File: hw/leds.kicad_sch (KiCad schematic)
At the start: 8 parts, among them Q4 SSM6N35AFE

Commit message: layout finished (draft)
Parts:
- added D7 (x2): LED_BARG, proj_footprints:LED_RGB_2504_horiz_barg, symbol Device:LED_BARG
- added Q4 (x4): SSM6N35AFE, proj_footprints:SOT-563-adjusted, symbol Device:Q_Dual_NMOS_S1G1D2S2G2D1
- added R10 (x2): 750, Resistor_SMD:R_0603_1608Metric, symbol Device:R_Small
- added R9 (x2): 2k, Resistor_SMD:R_0603_1608Metric, symbol Device:R_Small
- added R98 (x2): 230, Resistor_SMD:R_0603_1608Metric, symbol Device:R_Small
- Q4: symbol Device:Q_DUAL_NMOS_S1G1D2S2G2D1 -> Device:Q_Dual_NMOS_S1G1D2S2G2D1
- Q4: symbol Device:Q_DUAL_NMOS_S1G1D2S2G2D1 -> Device:Q_Dual_NMOS_S1G1D2S2G2D1; Manufacturer Toshiba -> (none)
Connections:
- net +5V: now also D7.2 (A), D7.2 (A)
- net GND: now also Q4.1 (S), Q4.1 (S), Q4.1 (S), Q4.1 (S), Q4.4 (S), Q4.4 (S)
- new net: D7.3 (RK), R10.1 (x2)
- new net: Q4.6 (D), R10.2
- new net: D7.1 (BK), R98.1 (x2)
- new net: D7.4 (GK), R9.1 (x2)
- new net: Q4.6 (D), R9.2 (x2)
- new net: Q4.3 (D), R98.2
- new net: Q4.6 (D), R98.2
- new net: Q4.3 (D), R10.2
- new net LED_CHA_B: Q4.2 (G)
- new net LED_CHA_G: Q4.2 (G)
- new net LED_CHA_R: Q4.5 (G)
- new net LED_CHB_B: Q4.5 (G)
- new net LED_CHB_G: Q4.2 (G)
- new net LED_CHB_R: Q4.2 (G)

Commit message: finished routing; DRC passes (except for 1 hole violation at push-button)
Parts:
- Q4: Manufacturer (none) -> Toshiba; Part (none) -> SSM6N35AFE
- Q4: Part (none) -> SSM6N35AFE
- R24: Manufacturer Yageo -> (none); Part RT0603FRE0710KL -> (none)
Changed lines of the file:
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@@
       (effects (font (size 1.27 1.27)) hide)
     )
-    (property "Part" "RT0603FRE0710KL" (at 95.885 40.005 90)
-      (effects (font (size 1.27 1.27)) hide)
-    )
-    (property "Manufacturer" "Yageo" (at 95.885 40.005 90)
+    (property "Part" "" (at 95.885 40.005 90)
+      (effects (font (size 1.27 1.27)) hide)
+    )
+    (property "Manufacturer" "" (at 95.885 40.005 90)
       (effects (font (size 1.27 1.27)) hide)
     )
@@
     )
     (property "Datasheet" "~" (at 177.8 116.84 0)
+      (effects (font (size 1.27 1.27)) hide)
+    )
+    (property "Manufacturer" "Toshiba" (at 172.72 116.84 0)
+      (effects (font (size 1.27 1.27)) hide)
+    )
+    (property "Part" "SSM6N35AFE" (at 172.72 116.84 0)
       (effects (font (size 1.27 1.27)) hide)
     )
@@
       (effects (font (size 1.27 1.27)) hide)
     )
+    (property "Manufacturer" "Toshiba" (at 80.645 135.89 0)
+      (effects (font (size 1.27 1.27)) hide)
+    )
+    (property "Part" "SSM6N35AFE" (at 80.645 135.89 0)
+      (effects (font (size 1.27 1.27)) hide)
+    )
     (pin "1")
     (pin "2")
@@
       (effects (font (size 1.27 1.27)) hide)
     )
+    (property "Part" "SSM6N35AFE" (at 80.645 56.515 0)
+      (effects (font (size 1.27 1.27)) hide)
+    )
     (pin "1")
     (pin "2")
@@
       (effects (font (size 1.27 1.27)) hide)
     )
+    (property "Manufacturer" "Toshiba" (at 80.645 116.84 0)
+      (effects (font (size 1.27 1.27)) hide)
+    )
+    (property "Part" "SSM6N35AFE" (at 80.645 116.84 0)
+      (effects (font (size 1.27 1.27)) hide)
+    )
     (pin "1")
     (pin "2")
@@
       (effects (font (size 1.27 1.27)) hide)
     )
+    (property "Manufacturer" "Toshiba" (at 80.645 94.615 0)
+      (effects (font (size 1.27 1.27)) hide)
+    )
+    (property "Part" "SSM6N35AFE" (at 80.645 94.615 0)
+      (effects (font (size 1.27 1.27)) hide)
+    )
     (pin "1")
     (pin "2")
@@
       (effects (font (size 1.27 1.27)) hide)
     )
+    (property "Manufacturer" "Toshiba" (at 80.645 75.565 0)
+      (effects (font (size 1.27 1.27)) hide)
+    )
+    (property "Part" "SSM6N35AFE" (at 80.645 75.565 0)
+      (effects (font (size 1.27 1.27)) hide)
+    )
     (pin "1")
     (pin "2")
@@
       (effects (font (size 1.27 1.27)) hide)
     )
+    (property "Manufacturer" "Toshiba" (at 172.72 154.94 0)
+      (effects (font (size 1.27 1.27)) hide)
+    )
+    (property "Part" "SSM6N35AFE" (at 172.72 154.94 0)
+      (effects (font (size 1.27 1.27)) hide)
+    )
     (pin "1")
     (pin "2")
@@
       (effects (font (size 1.27 1.27)) hide)
     )
+    (property "Manufacturer" "Toshiba" (at 80.645 154.94 0)
+      (effects (font (size 1.27 1.27)) hide)
+    )
+    (property "Part" "SSM6N35AFE" (at 80.645 154.94 0)
+      (effects (font (size 1.27 1.27)) hide)
+    )
     (pin "1")
     (pin "2")
@@
       (effects (font (size 1.27 1.27)) hide)
     )
+    (property "Manufacturer" "Toshiba" (at 172.72 135.89 0)
+      (effects (font (size 1.27 1.27)) hide)
+    )
+    (property "Part" "SSM6N35AFE" (at 172.72 135.89 0)
+      (effects (font (size 1.27 1.27)) hide)
+    )
     (pin "1")
     (pin "2")
@@
       (effects (font (size 1.27 1.27)) hide)
     )
+    (property "Manufacturer" "Toshiba" (at 81.915 37.465 0)
+      (effects (font (size 1.27 1.27)) hide)
+    )
+    (property "Part" "SSM6N35AFE" (at 81.915 37.465 0)
+      (effects (font (size 1.27 1.27)) hide)
+    )

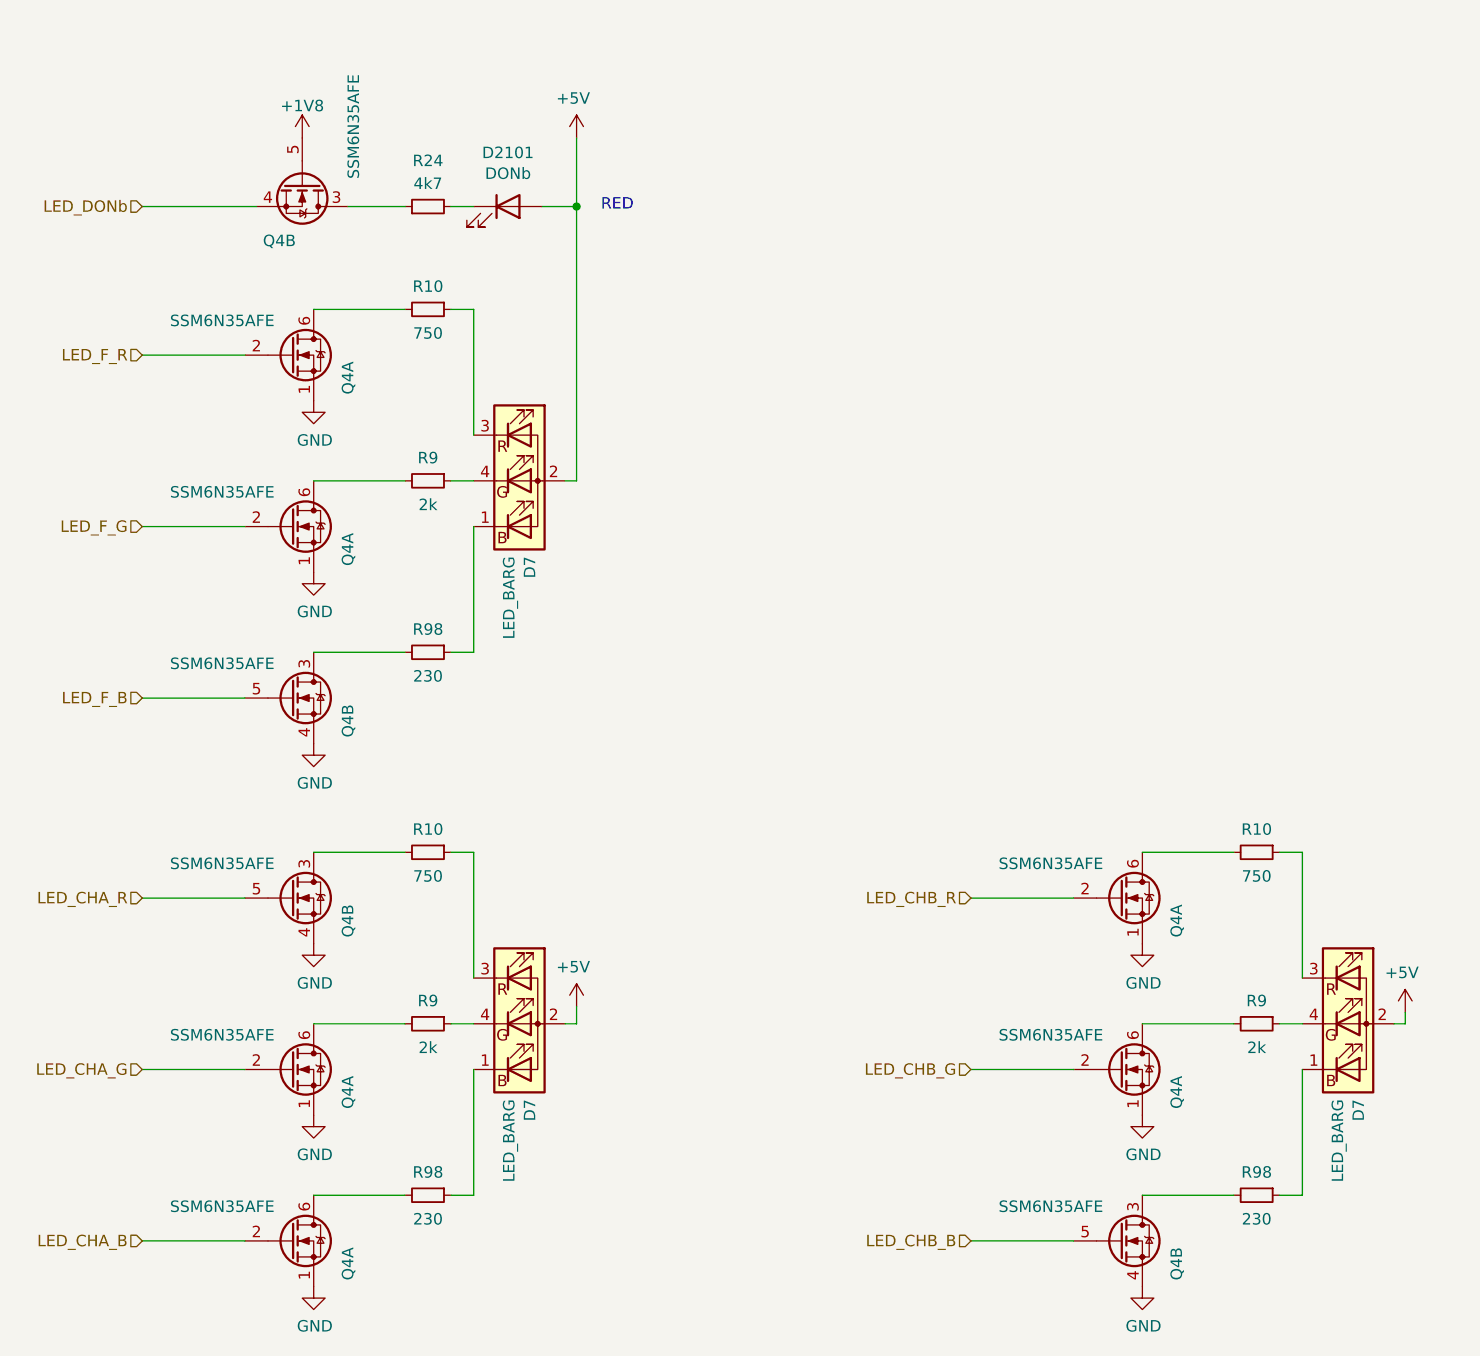
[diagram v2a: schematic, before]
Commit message: added 2nd front led; more keepouts around signal lines
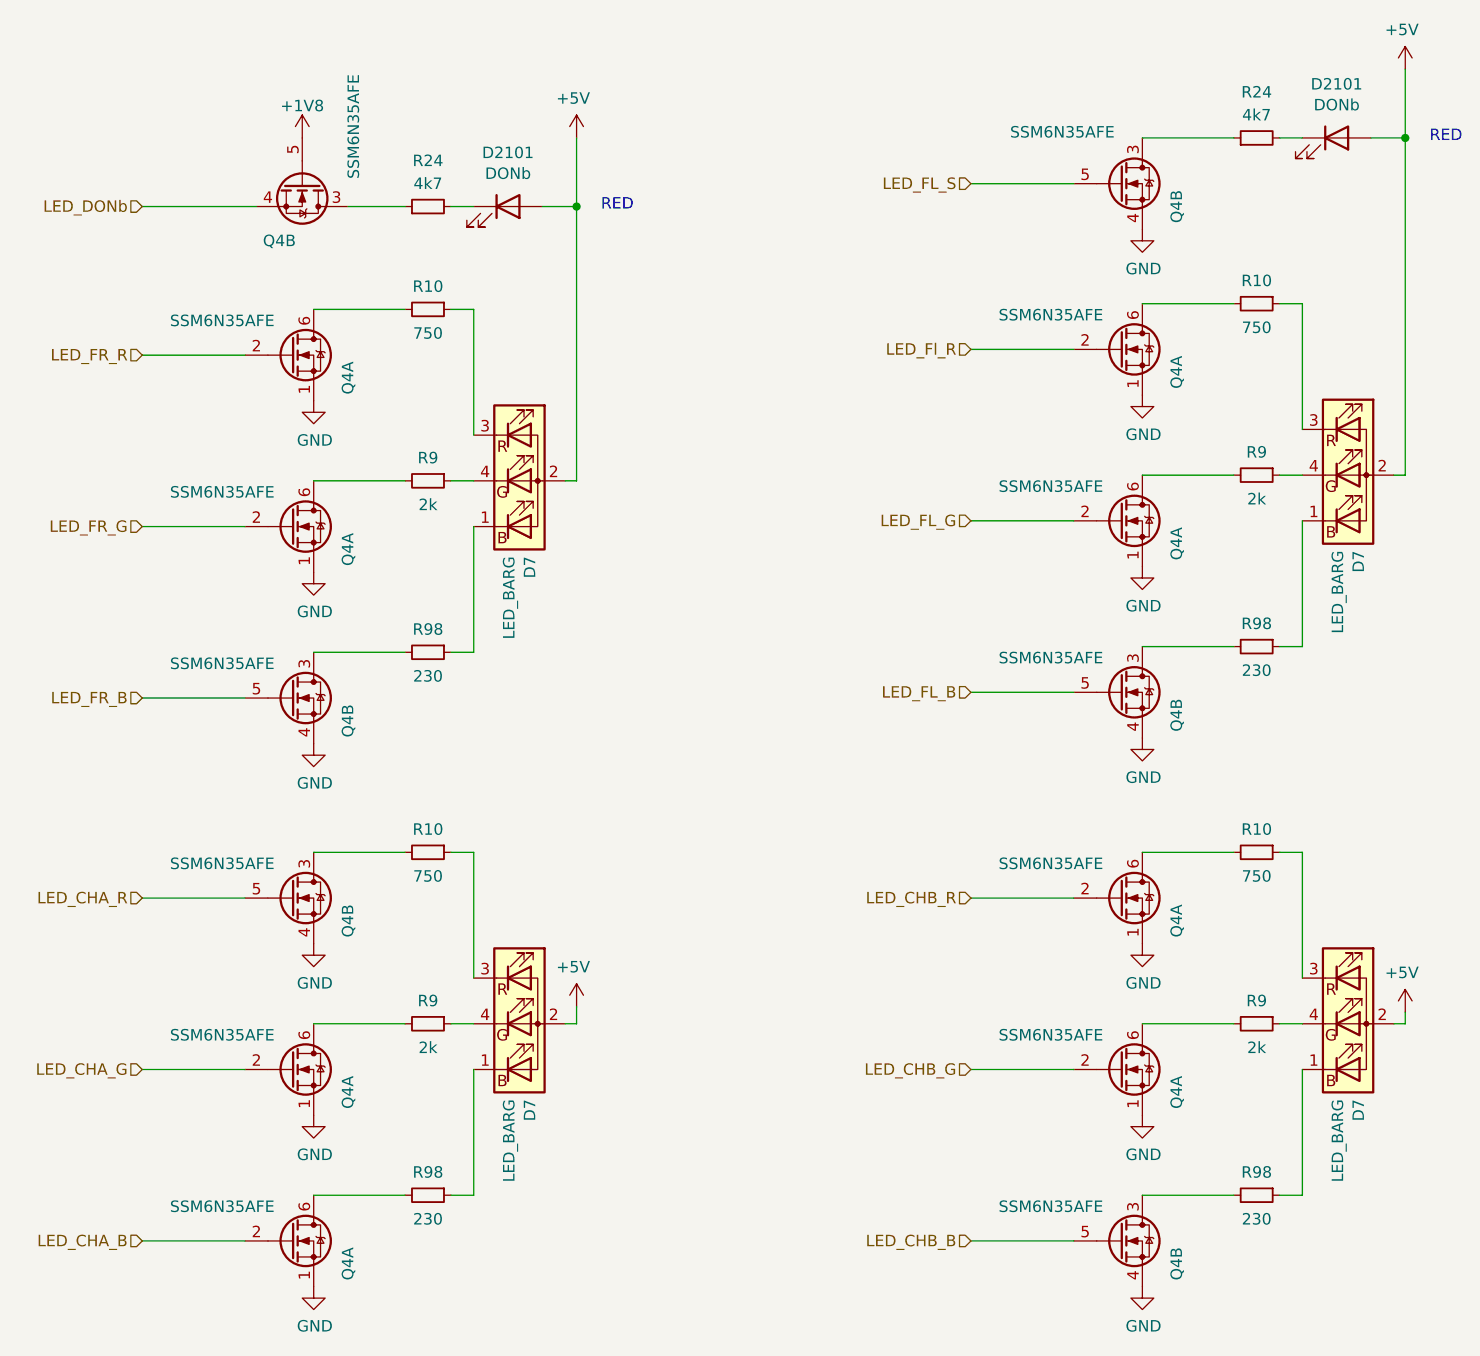
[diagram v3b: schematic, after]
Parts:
- added D2101: DONb, LED_SMD:LED_0603_1608Metric, symbol Device:LED
- added D7: LED_BARG, proj_footprints:LED_RGB_2504_horiz_barg, symbol Device:LED_BARG
- added Q4 (x2): SSM6N35AFE, proj_footprints:SOT-563-adjusted, symbol Device:Q_Dual_NMOS_S1G1D2S2G2D1
- added R10: 750, Resistor_SMD:R_0603_1608Metric, symbol Device:R_Small
- added R24: 4k7, Resistor_SMD:R_0603_1608Metric, symbol Device:R_Small
- added R9: 2k, Resistor_SMD:R_0603_1608Metric, symbol Device:R_Small
- added R98: 230, Resistor_SMD:R_0603_1608Metric, symbol Device:R_Small
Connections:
- net +5V: now also D2101.2 (A), D7.2 (A)
- net GND: now also Q4.1 (S), Q4.1 (S), Q4.4 (S), Q4.4 (S)
- net LED_F_B renamed LED_FR_B
- net LED_F_G renamed LED_FR_G
- net LED_F_R renamed LED_FR_R
- new net: D7.3 (RK), R10.1
- new net: Q4.6 (D), R10.2
- new net: D2101.1 (K), R24.2
- new net: Q4.3 (D), R24.1
- new net: D7.1 (BK), R98.1
- new net: D7.4 (GK), R9.1
- new net: Q4.3 (D), R98.2
- new net: Q4.6 (D), R9.2
- new net LED_FL_B: Q4.5 (G)
- new net LED_FL_G: Q4.2 (G)
- new net LED_FL_S: Q4.5 (G)
- new net LED_Fl_R: Q4.2 (G)

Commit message: standardized resistor/capacitor values
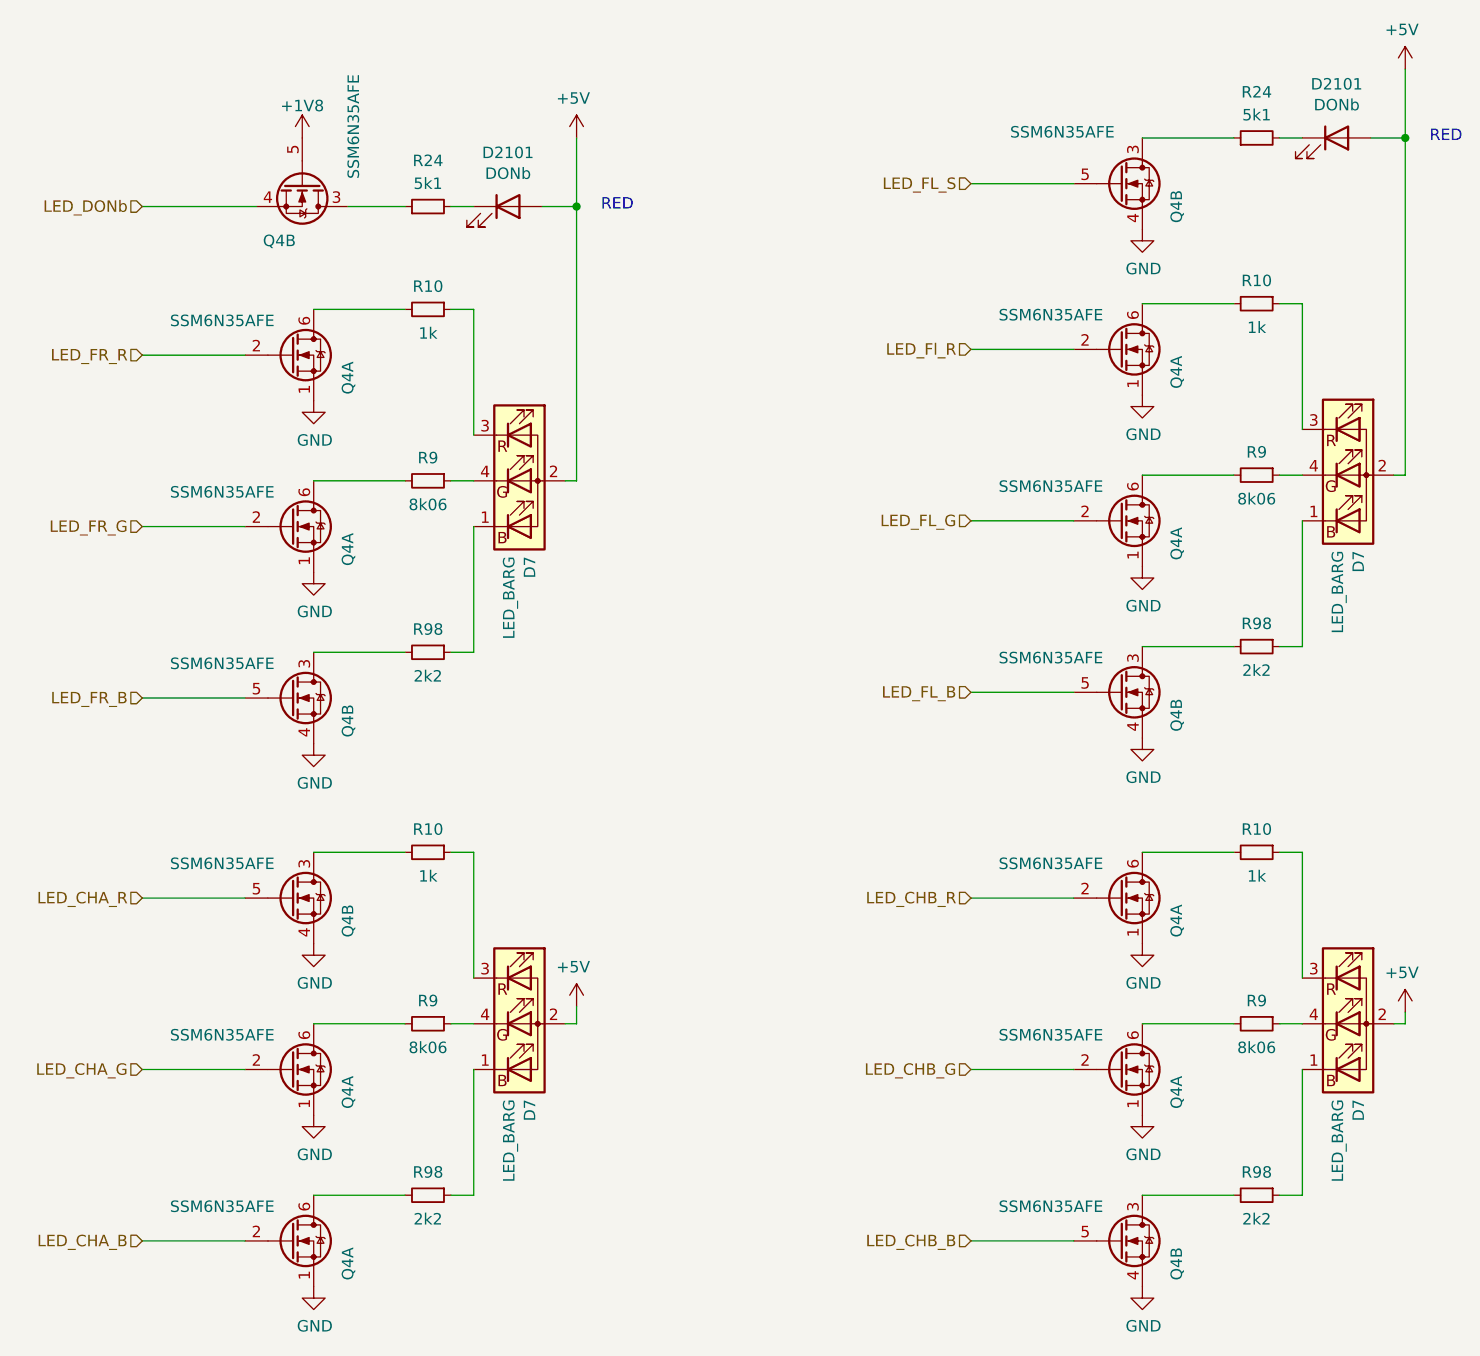
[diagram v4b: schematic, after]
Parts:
- R10: value 750 -> 1k
- R24: value 4k7 -> 5k1
- R9: value 2k -> 8k06
- R98: value 230 -> 2k2
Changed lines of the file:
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@@
       (effects (font (size 1.27 1.27)))
     )
-    (property "Value" "750" (at 187.96 114.427 90)
+    (property "Value" "1k" (at 187.96 114.427 90)
       (effects (font (size 1.27 1.27)))
     )
@@
       (effects (font (size 1.27 1.27)))
     )
-    (property "Value" "750" (at 187.96 53.467 90)
+    (property "Value" "1k" (at 187.96 53.467 90)
       (effects (font (size 1.27 1.27)))
     )
@@
       (effects (font (size 1.27 1.27)))
     )
-    (property "Value" "2k" (at 187.96 133.477 90)
+    (property "Value" "8k06" (at 187.96 133.477 90)
       (effects (font (size 1.27 1.27)))
     )
@@
       (effects (font (size 1.27 1.27)))
     )
-    (property "Value" "4k7" (at 95.885 37.465 90)
+    (property "Value" "5k1" (at 95.885 37.465 90)
       (effects (font (size 1.27 1.27)))
     )
@@
       (effects (font (size 1.27 1.27)))
     )
-    (property "Value" "230" (at 187.96 152.527 90)
+    (property "Value" "2k2" (at 187.96 152.527 90)
       (effects (font (size 1.27 1.27)))
     )
@@
       (effects (font (size 1.27 1.27)))
     )
-    (property "Value" "230" (at 95.885 152.527 90)
+    (property "Value" "2k2" (at 95.885 152.527 90)
       (effects (font (size 1.27 1.27)))
     )
@@
       (effects (font (size 1.27 1.27)))
     )
-    (property "Value" "750" (at 95.885 54.102 90)
+    (property "Value" "1k" (at 95.885 54.102 90)
       (effects (font (size 1.27 1.27)))
     )
@@
       (effects (font (size 1.27 1.27)))
     )
-    (property "Value" "4k7" (at 187.96 29.845 90)
+    (property "Value" "5k1" (at 187.96 29.845 90)
       (effects (font (size 1.27 1.27)))
     )
@@
       (effects (font (size 1.27 1.27)))
     )
-    (property "Value" "230" (at 187.96 91.567 90)
+    (property "Value" "2k2" (at 187.96 91.567 90)
       (effects (font (size 1.27 1.27)))
     )
@@
       (effects (font (size 1.27 1.27)))
     )
-    (property "Value" "2k" (at 95.885 73.152 90)
+    (property "Value" "8k06" (at 95.885 73.152 90)
       (effects (font (size 1.27 1.27)))
     )
@@
       (effects (font (size 1.27 1.27)))
     )
-    (property "Value" "230" (at 95.885 92.202 90)
+    (property "Value" "2k2" (at 95.885 92.202 90)
       (effects (font (size 1.27 1.27)))
     )
@@
       (effects (font (size 1.27 1.27)))
     )
-    (property "Value" "2k" (at 95.885 133.477 90)
+    (property "Value" "8k06" (at 95.885 133.477 90)
       (effects (font (size 1.27 1.27)))
     )
@@
       (effects (font (size 1.27 1.27)))
     )
-    (property "Value" "750" (at 95.885 114.427 90)
+    (property "Value" "1k" (at 95.885 114.427 90)
       (effects (font (size 1.27 1.27)))
     )
@@
       (effects (font (size 1.27 1.27)))
     )
-    (property "Value" "2k" (at 187.96 72.517 90)
-      (effects (font (size 1.27 1.27)))
-    )
+    (property "Value" "8k06" (at 187.96 72.517 90)
+      (effects (font (size 1.27 1.27)))
+    )
